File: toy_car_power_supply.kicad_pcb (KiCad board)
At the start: 2 copper layers, 40.4 x 44.5 mm, 17 parts, among them J1 Barrel_Jack_Switch, J2 Screw_Terminal_01x02, J3 Screw_Terminal_01x02, J4 Conn_01x03_Pin, J5 Conn_01x02_Pin, J6 Conn_01x03_Pin, J7 Conn_01x02_Pin, SW1 SW_Wuerth_450301014042, U1 LM317_TO-220, U2 LM7805_TO220

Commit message: Updated track width for all tracks
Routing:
- net /PWR_output_bot: track 16.3 -> 24.5 mm
- net /12V: track 55.1 -> 62.6 mm
- net GND: track 147.4 -> 153.4 mm
- net /3.3V: track 151.5 -> 149.2 mm
- net /PWR_output_top: track 24.8 -> 26.8 mm

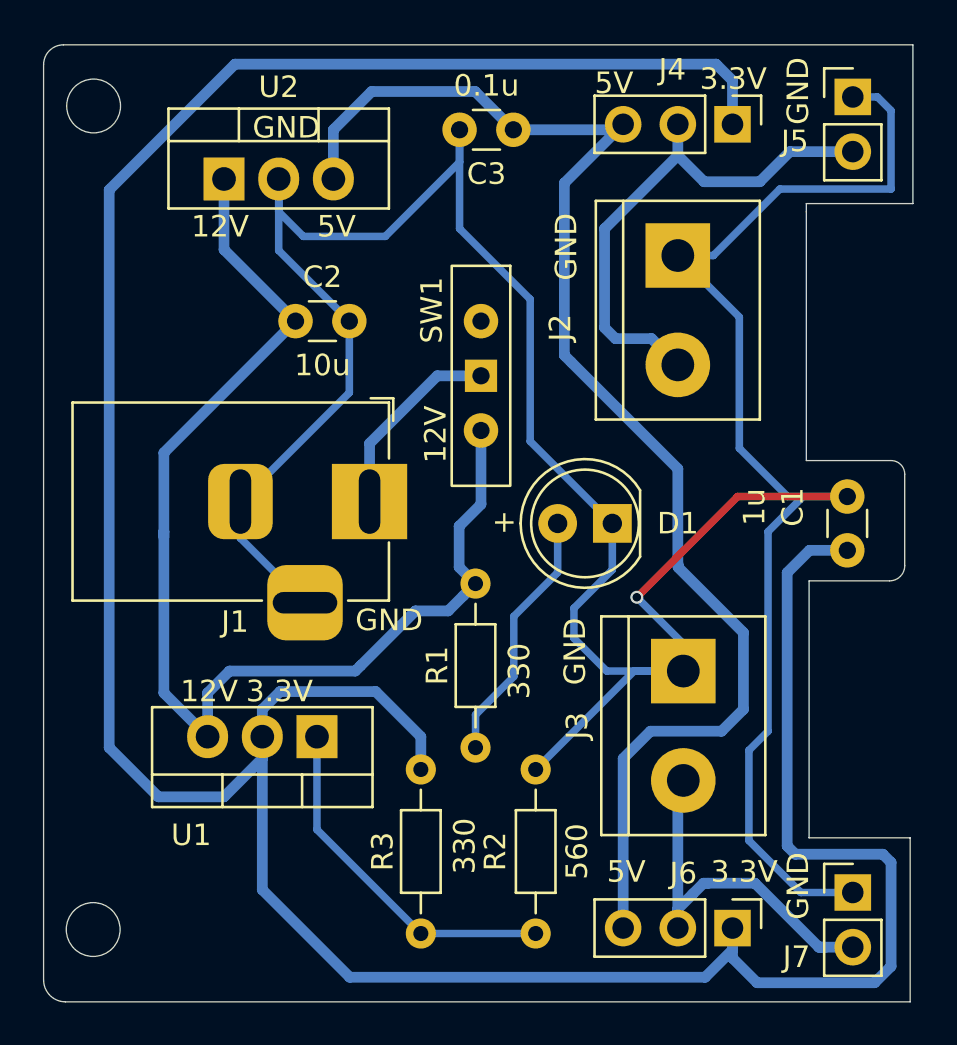
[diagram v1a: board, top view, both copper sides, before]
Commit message: Updated with custom switch with 4 pin
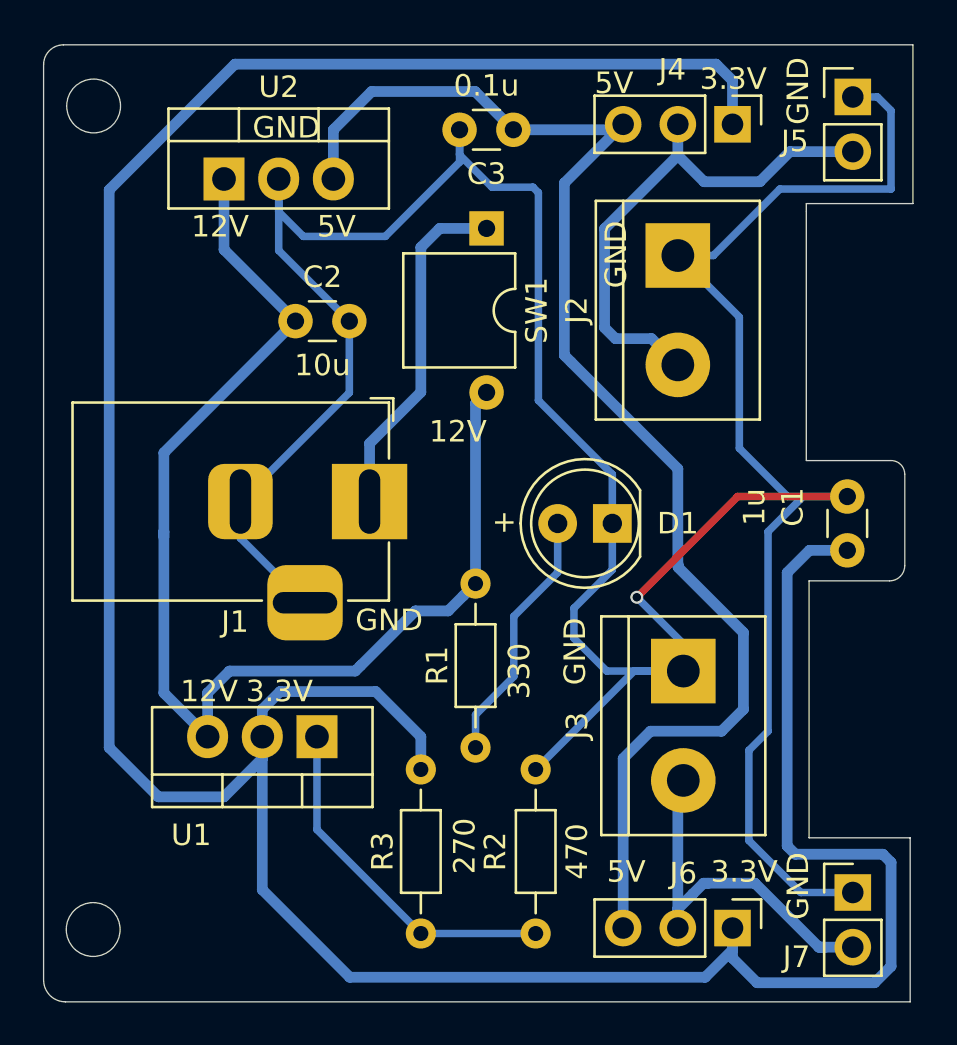
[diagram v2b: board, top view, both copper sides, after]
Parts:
- R2: value 560 -> 470
- R3: value 330 -> 270
- SW1: value SW_Wuerth_450301014042 -> SW_DIP_x02; footprint Button_Switch_THT:SW_Slide-03_Wuerth-WS-SLTV_10x2.5x6.4_P2.54mm -> custom_switch:DIP-4_W7.62mm
- moved SW1 6.85 mm to (130.3, 82.3)
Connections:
- SW1 pad 2: unconnected-(SW1-C-Pad2) -> /12V
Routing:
- net /PWR_input: track 9.18 -> 16.2 mm
- net /12V: track 62.6 -> 63.8 mm
- net GND: track 153.4 -> 154.5 mm

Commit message: Remove redundant library
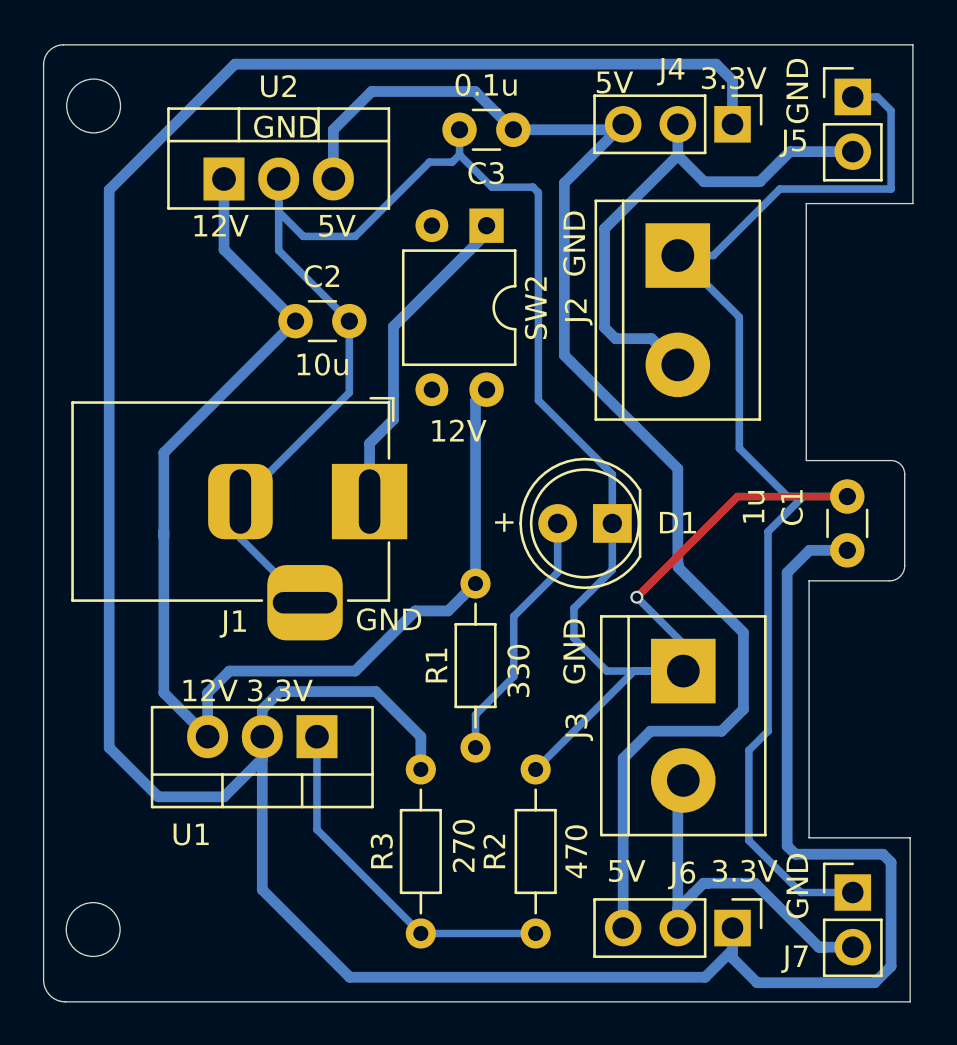
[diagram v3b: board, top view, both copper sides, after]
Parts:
- removed SW1: SW_DIP_x02, custom_switch:DIP-4_W7.62mm
- added SW2: Slider Switch, custom_switch:DIP-4_W7.62mm, F.Cu at (130.3, 82.2)
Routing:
- net GND: track 154.5 -> 153.1 mm
- net /PWR_input: track 16.2 -> 15.1 mm

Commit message: Added conector for 12 v supply
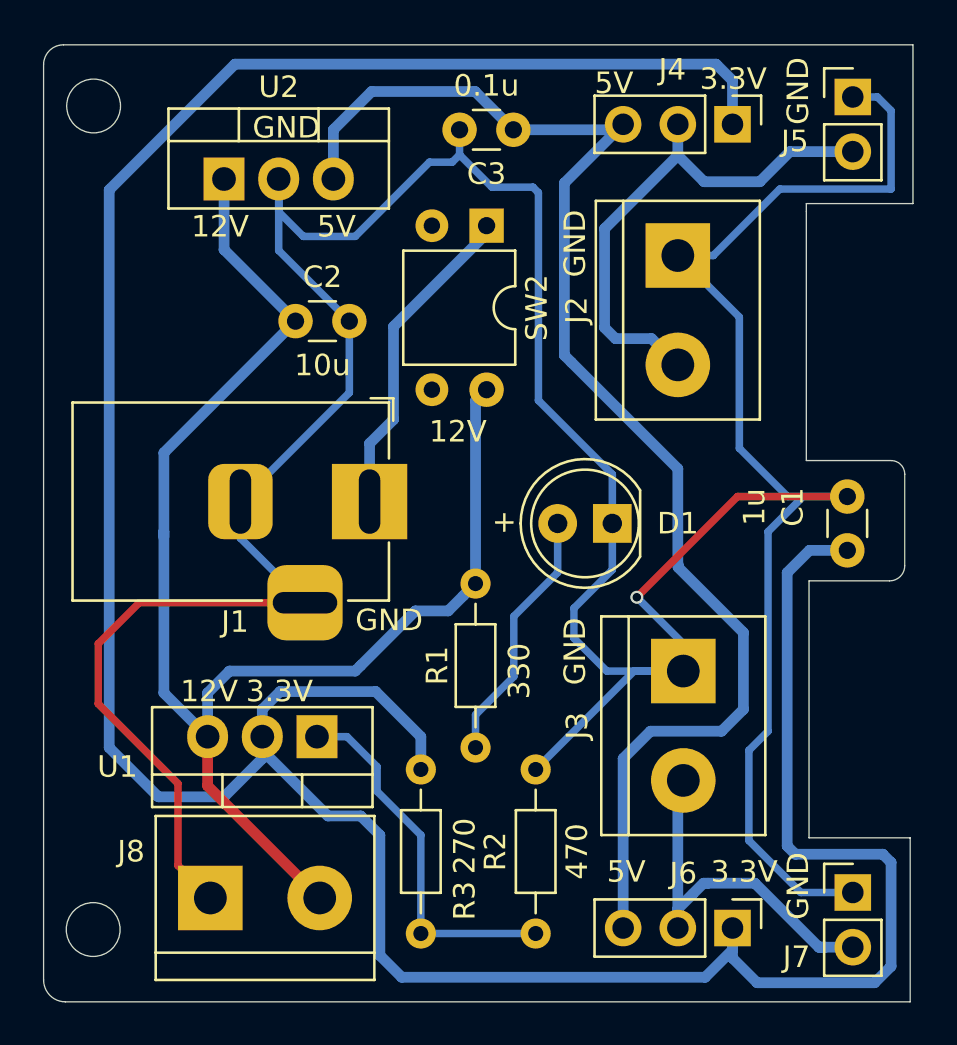
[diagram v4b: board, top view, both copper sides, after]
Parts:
- added J8: Screw_Terminal_01x02, TerminalBlock:TerminalBlock_bornier-2_P5.08mm, F.Cu at (117.5, 113.4)
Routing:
- net GND: track 153.1 -> 177.5 mm
- net /12V: track 64.0 -> 73.6 mm
- net Net-(U1-ADJ): track 16.5 -> 17.3 mm
- net /3.3V: track 149.2 -> 148.6 mm

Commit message: Updated pcb
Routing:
- net /12V: track 73.6 -> 74.8 mm
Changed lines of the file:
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@@
     (pcbplotparams
       (layerselection 0x0000000_fffffffe)
-      (plot_on_all_layers_selection 0x0005054_00000000)
+      (plot_on_all_layers_selection 0x0000054_00000000)
       (disableapertmacros false)
       (usegerberextensions true)
@@
   (via (at 137.287 99.441) (size 0.6) (drill 0.4) (layers "F.Cu" "B.Cu") (net 1))
   (segment (start 132.461 80.391) (end 130.556 80.391) (width 0.35) (layer "B.Cu") (net 1))
-  (segment (start 142.494 110.744) (end 142.494 106.553) (width 0.35) (layer "B.Cu") (net 1))
-  (segment (start 143.383 105.664) (end 143.383 96.393) (width 0.35) (layer "B.Cu") (net 1))
+  (segment (start 142.24 107.061) (end 142.24 110.49) (width 0.35) (layer "B.Cu") (net 1))
+  (segment (start 148.463 76.2) (end 147.32 76.2) (width 0.35) (layer "B.Cu") (net 1))
   (segment (start 132.715 80.645) (end 132.461 80.391) (width 0.35) (layer "B.Cu") (net 1))
   (segment (start 142.0495 92.5195) (end 144.292 94.762) (width 0.35) (layer "B.Cu") (net 1))
+  (segment (start 144.907 113.157) (end 147.32 113.157) (width 0.35) (layer "B.Cu") (net 1))
   (segment (start 123.932 86.614) (end 123.932 89.936) (width 0.35) (layer "B.Cu") (net 1))
   (segment (start 132.715 90.297) (end 132.715 80.645) (width 0.35) (layer "B.Cu") (net 1))
@@
   (segment (start 139.446 101.6) (end 137.287 99.441) (width 0.35) (layer "B.Cu") (net 1))
   (segment (start 136.149 98.166) (end 134.366 99.949) (width 0.35) (layer "B.Cu") (net 1))
-  (segment (start 149.098 80.478) (end 143.931 80.478) (width 0.35) (layer "B.Cu") (net 1))
-  (segment (start 142.494 106.553) (end 143.383 105.664) (width 0.35) (layer "B.Cu") (net 1))
   (segment (start 124.206 82.677) (end 127.655 79.228) (width 0.35) (layer "B.Cu") (net 1))
+  (segment (start 142.24 110.49) (end 144.907 113.157) (width 0.35) (layer "B.Cu") (net 1))
   (segment (start 137.16 102.87) (end 139.446 102.87) (width 0.35) (layer "B.Cu") (net 1))
   (segment (start 134.366 101.346) (end 135.89 102.87) (width 0.35) (layer "B.Cu") (net 1))
@@
   (segment (start 120.65 80.01) (end 120.65 83.332) (width 0.35) (layer "B.Cu") (net 1))
   (segment (start 144.907 94.869) (end 145.014 94.762) (width 0.25) (layer "B.Cu") (net 1))
-  (segment (start 143.931 80.478) (end 140.843 83.566) (width 0.35) (layer "B.Cu") (net 1))
   (segment (start 128.711 79.228) (end 129.052 78.887) (width 0.35) (layer "B.Cu") (net 1))
-  (segment (start 149.098 76.835) (end 149.098 80.478) (width 0.35) (layer "B.Cu") (net 1))
+  (segment (start 139.192 83.566) (end 141.478 83.566) (width 0.35) (layer "B.Cu") (net 1))
   (segment (start 136.149 96.012) (end 136.149 93.731) (width 0.35) (layer "B.Cu") (net 1))
-  (segment (start 140.843 83.566) (end 139.192 83.566) (width 0.35) (layer "B.Cu") (net 1))
-  (segment (start 143.383 96.393) (end 144.907 94.869) (width 0.35) (layer "B.Cu") (net 1))
+  (segment (start 149.098 80.478) (end 149.098 76.835) (width 0.35) (layer "B.Cu") (net 1))
   (segment (start 136.149 93.731) (end 132.715 90.297) (width 0.35) (layer "B.Cu") (net 1))
+  (segment (start 144.566 80.478) (end 149.098 80.478) (width 0.35) (layer "B.Cu") (net 1))
   (segment (start 127.655 79.228) (end 128.711 79.228) (width 0.35) (layer "B.Cu") (net 1))
   (segment (start 142.0495 86.4235) (end 142.0495 92.5195) (width 0.35) (layer "B.Cu") (net 1))
+  (segment (start 149.098 76.835) (end 148.463 76.2) (width 0.35) (layer "B.Cu") (net 1))
   (segment (start 123.932 89.936) (end 118.872 94.996) (width 0.35) (layer "B.Cu") (net 1))
+  (segment (start 143.256 96.52) (end 143.256 106.045) (width 0.35) (layer "B.Cu") (net 1))
   (segment (start 118.872 96.696) (end 121.872 99.696) (width 0.35) (layer "B.Cu") (net 1))
   (segment (start 121.793 82.677) (end 124.206 82.677) (width 0.35) (layer "B.Cu") (net 1))
   (segment (start 134.366 99.949) (end 134.366 101.346) (width 0.35) (layer "B.Cu") (net 1))
-  (segment (start 147.32 113.157) (end 144.907 113.157) (width 0.35) (layer "B.Cu") (net 1))
   (segment (start 120.65 81.534) (end 121.793 82.677) (width 0.35) (layer "B.Cu") (net 1))
   (segment (start 144.292 94.762) (end 147.066 94.762) (width 0.35) (layer "B.Cu") (net 1))
   (segment (start 139.192 83.566) (end 142.0495 86.4235) (width 0.35) (layer "B.Cu") (net 1))
   (segment (start 139.446 102.87) (end 139.446 101.6) (width 0.35) (layer "B.Cu") (net 1))
-  (segment (start 148.463 76.2) (end 149.098 76.835) (width 0.35) (layer "B.Cu") (net 1))
-  (segment (start 144.907 113.157) (end 142.494 110.744) (width 0.35) (layer "B.Cu") (net 1))
+  (segment (start 144.907 94.869) (end 143.256 96.52) (width 0.35) (layer "B.Cu") (net 1))
+  (segment (start 141.478 83.566) (end 144.566 80.478) (width 0.35) (layer "B.Cu") (net 1))
   (segment (start 132.588 107.442) (end 137.16 102.87) (width 0.35) (layer "B.Cu") (net 1))
-  (segment (start 147.32 76.2) (end 148.463 76.2) (width 0.35) (layer "B.Cu") (net 1))
+  (segment (start 143.256 106.045) (end 142.24 107.061) (width 0.35) (layer "B.Cu") (net 1))
   (segment (start 142.24 114.3) (end 141.732 114.808) (width 0.35) (layer "F.Cu") (net 2))
   (segment (start 115.062 108.712) (end 118.11 108.712) (width 0.5) (layer "B.Cu") (net 2))
@@
   (segment (start 122.555 113.411) (end 117.348 108.204) (width 0.5) (layer "F.Cu") (net 3))
   (segment (start 118.11 83.292) (end 121.432 86.614) (width 0.5) (layer "B.Cu") (net 3))
+  (segment (start 129.794 100.838) (end 129.794 98.806) (width 0.5) (layer "B.Cu") (net 3))
   (segment (start 115.316 96.647) (end 115.316 103.886) (width 0.35) (layer "B.Cu") (net 3))
   (segment (start 115.316 103.886) (end 117.348 105.918) (width 0.5) (layer "B.Cu") (net 3))
+  (segment (start 117.348 103.886) (end 118.618 102.616) (width 0.5) (layer "B.Cu") (net 3))
+  (segment (start 117.348 105.918) (end 117.348 103.886) (width 0.5) (layer "B.Cu") (net 3))
   (segment (start 118.11 80.01) (end 118.11 83.292) (width 0.5) (layer "B.Cu") (net 3))
-  (segment (start 124.46 102.616) (end 127 100.076) (width 0.5) (layer "B.Cu") (net 3))
-  (segment (start 117.348 103.886) (end 118.364 102.87) (width 0.5) (layer "B.Cu") (net 3))
+  (segment (start 128.016 102.616) (end 129.794 100.838) (width 0.5) (layer "B.Cu") (net 3))
   (segment (start 129.794 98.806) (end 129.794 90.312) (width 0.5) (layer "B.Cu") (net 3))
-  (segment (start 129.2225 99.3775) (end 129.794 98.806) (width 0.5) (layer "B.Cu") (net 3))
-  (segment (start 118.364 102.87) (end 124.206 102.87) (width 0.5) (layer "B.Cu") (net 3))
+  (segment (start 118.618 102.616) (end 128.016 102.616) (width 0.5) (layer "B.Cu") (net 3))
   (segment (start 121.432 86.614) (end 115.316 92.73) (width 0.5) (layer "B.Cu") (net 3))
-  (segment (start 117.348 105.918) (end 117.348 103.886) (width 0.5) (layer "B.Cu") (net 3))
-  (segment (start 127 100.076) (end 128.524 100.076) (width 0.5) (layer "B.Cu") (net 3))
   (segment (start 115.316 96.393) (end 115.316 96.647) (width 0.5) (layer "B.Cu") (net 3))
   (segment (start 129.794 90.312) (end 130.307 89.799) (width 0.5) (layer "B.Cu") (net 3))
   (segment (start 115.316 92.73) (end 115.316 96.393) (width 0.5) (layer "B.Cu") (net 3))
-  (segment (start 128.524 100.076) (end 129.2225 99.3775) (width 0.5) (layer "B.Cu") (net 3))
   (segment (start 115.316 96.393) (end 115.316 103.886) (width 0.5) (layer "B.Cu") (net 3))
-  (segment (start 124.206 102.87) (end 124.46 102.616) (width 0.5) (layer "B.Cu") (net 3))
   (segment (start 133.9215 80.2005) (end 133.9215 88.2015) (width 0.5) (layer "B.Cu") (net 4))
   (segment (start 139.192 93.472) (end 139.192 97.907695) (width 0.5) (layer "B.Cu") (net 4))
